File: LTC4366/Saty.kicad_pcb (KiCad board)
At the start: 2 copper layers, 71 x 18.4 mm, 12 parts, among them J1 Conn_01x02, Q1 HUF76639S3S

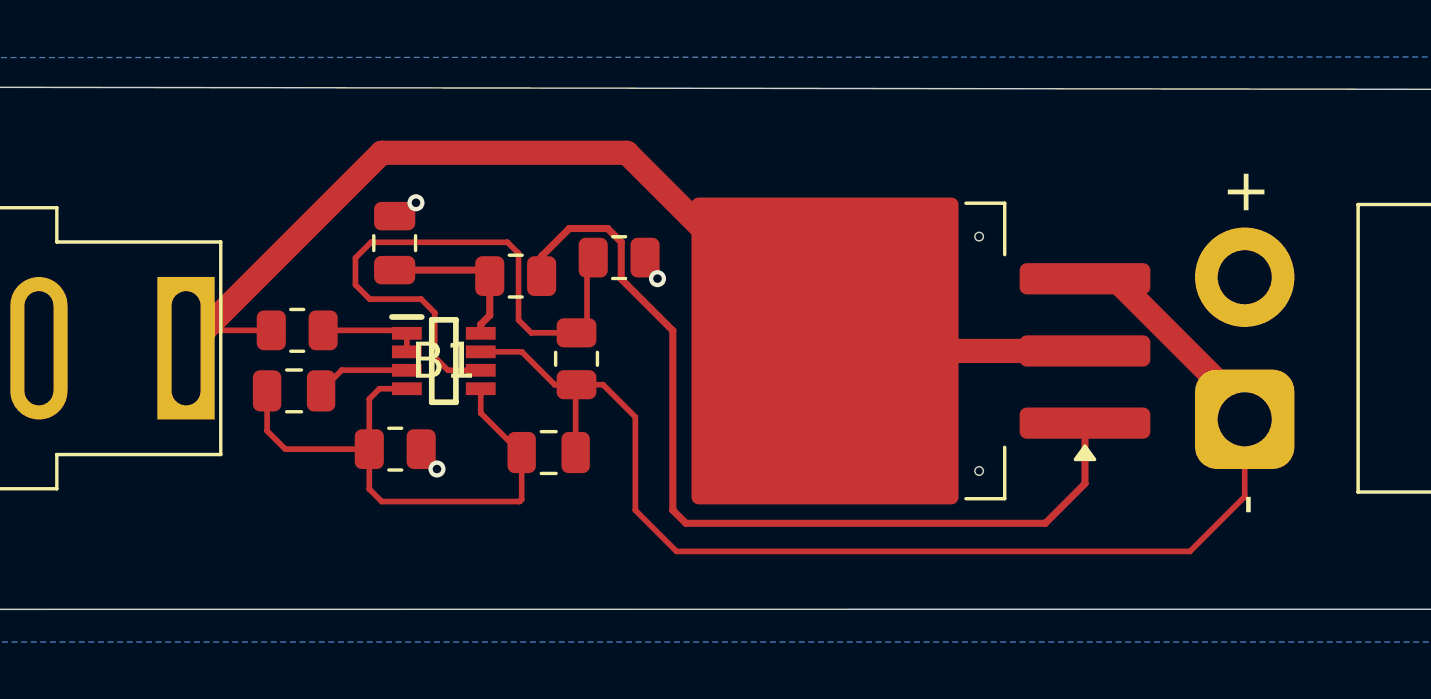
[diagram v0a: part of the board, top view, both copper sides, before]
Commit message: update the pcb layout of LTC4366
fixes clearance
fixes length
fixes track width
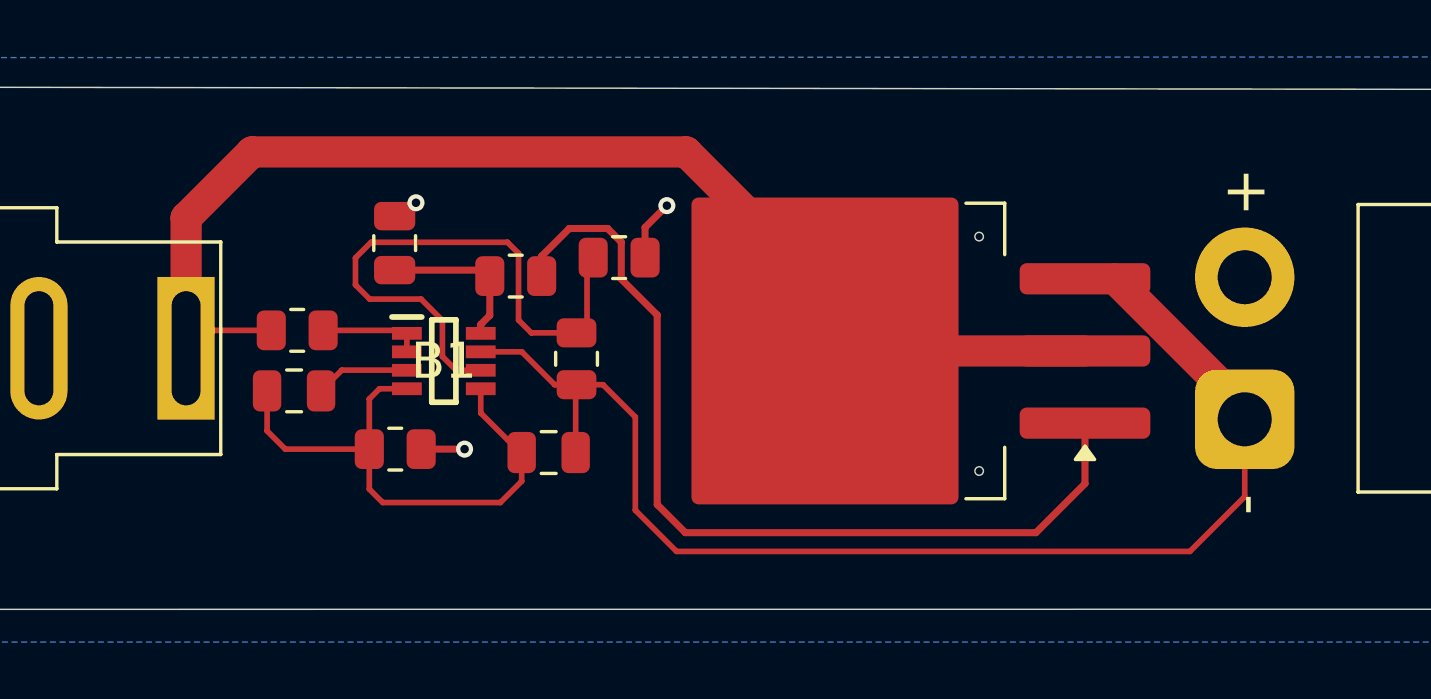
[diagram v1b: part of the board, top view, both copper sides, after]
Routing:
- net Net-(Q1-D): track 43.2 -> 47.2 mm
- net GND: track 0.00 -> 3.68 mm

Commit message: Add files via upload
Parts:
- moved J1 32.5 mm to (75.1, 116.2), turned to 180 degrees
- moved SC1 27.1 mm to (95.3, 115.1), turned to 90 degrees
- moved Q1 3.86 mm to (97.4, 107.0), turned to 0 degrees
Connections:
- J1 pad 1: /Vin LTC4162 -> GND
- J1 pad 2: GND -> /Vin LTC4162
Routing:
- net Net-(Q1-G): track 32.2 -> 10.3 mm
- net /Vin LTC4162: track 47.2 -> 25.8 mm
- net Net-(Q1-D): track 47.2 -> 56.9 mm
- net GND: track 3.68 -> 4.64 mm
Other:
- board size 71 x 18.4 mm -> 36 x 33.8 mm

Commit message: Add files via upload
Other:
- outline, holes or cut-outs redrawn
